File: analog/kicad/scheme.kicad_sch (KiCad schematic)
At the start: 23 parts, among them J1 Barrel_Jack_Switch, U1 LM7805_TO220, U2 LM324

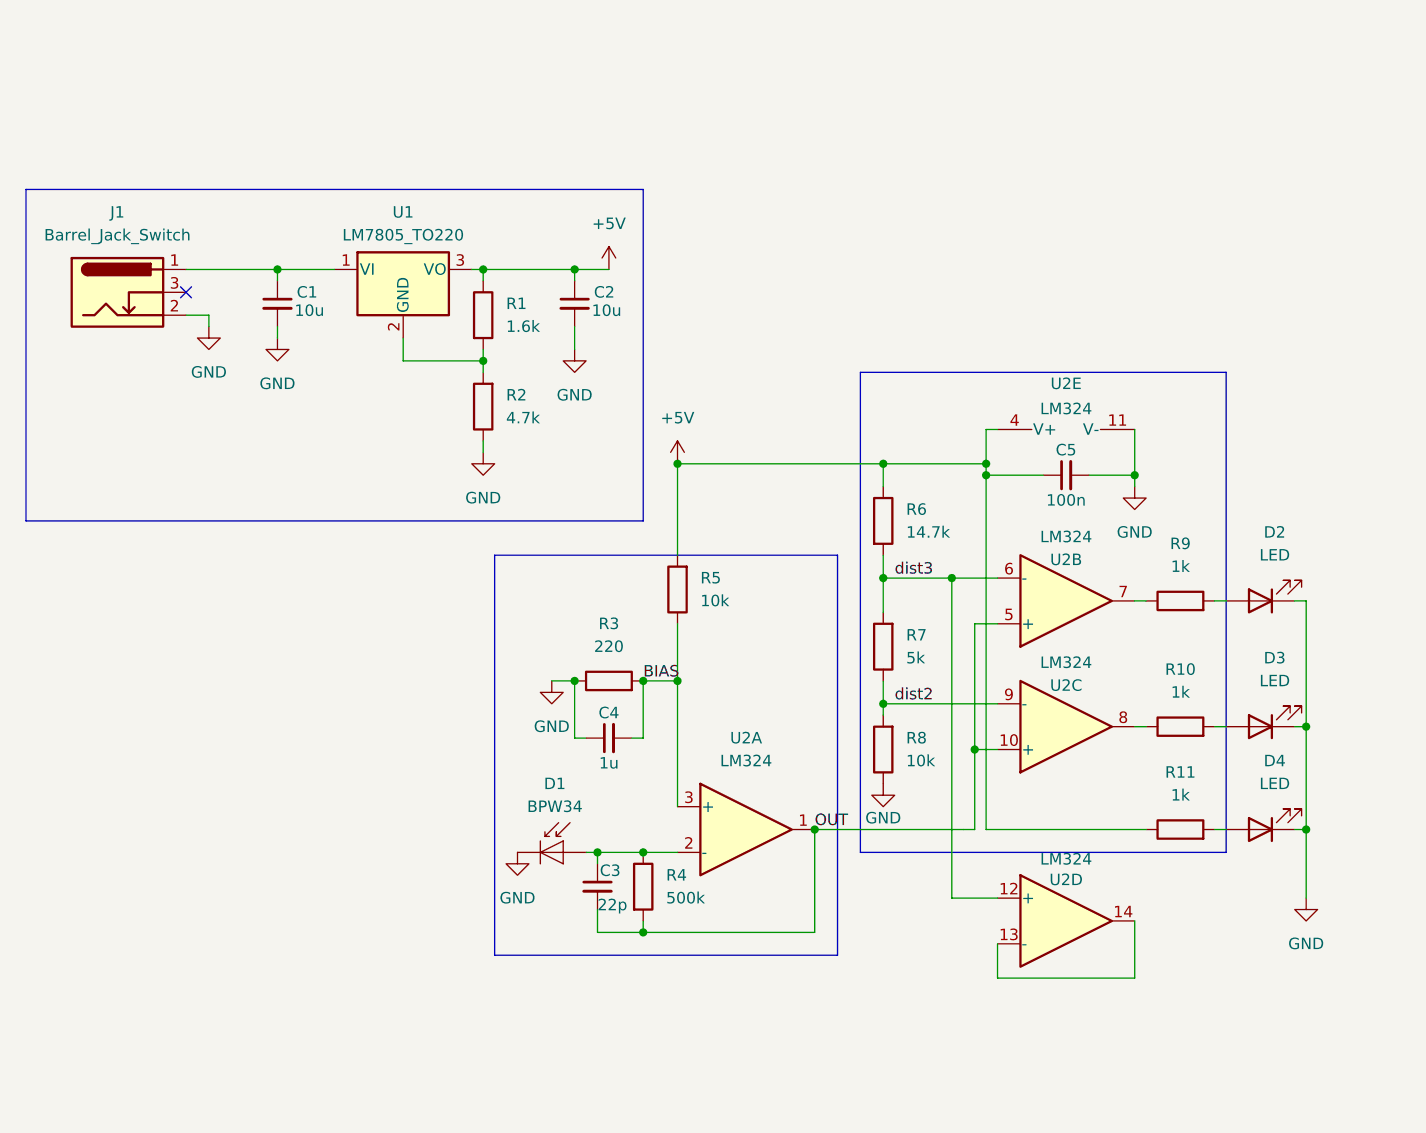
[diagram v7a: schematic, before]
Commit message: pwr good led
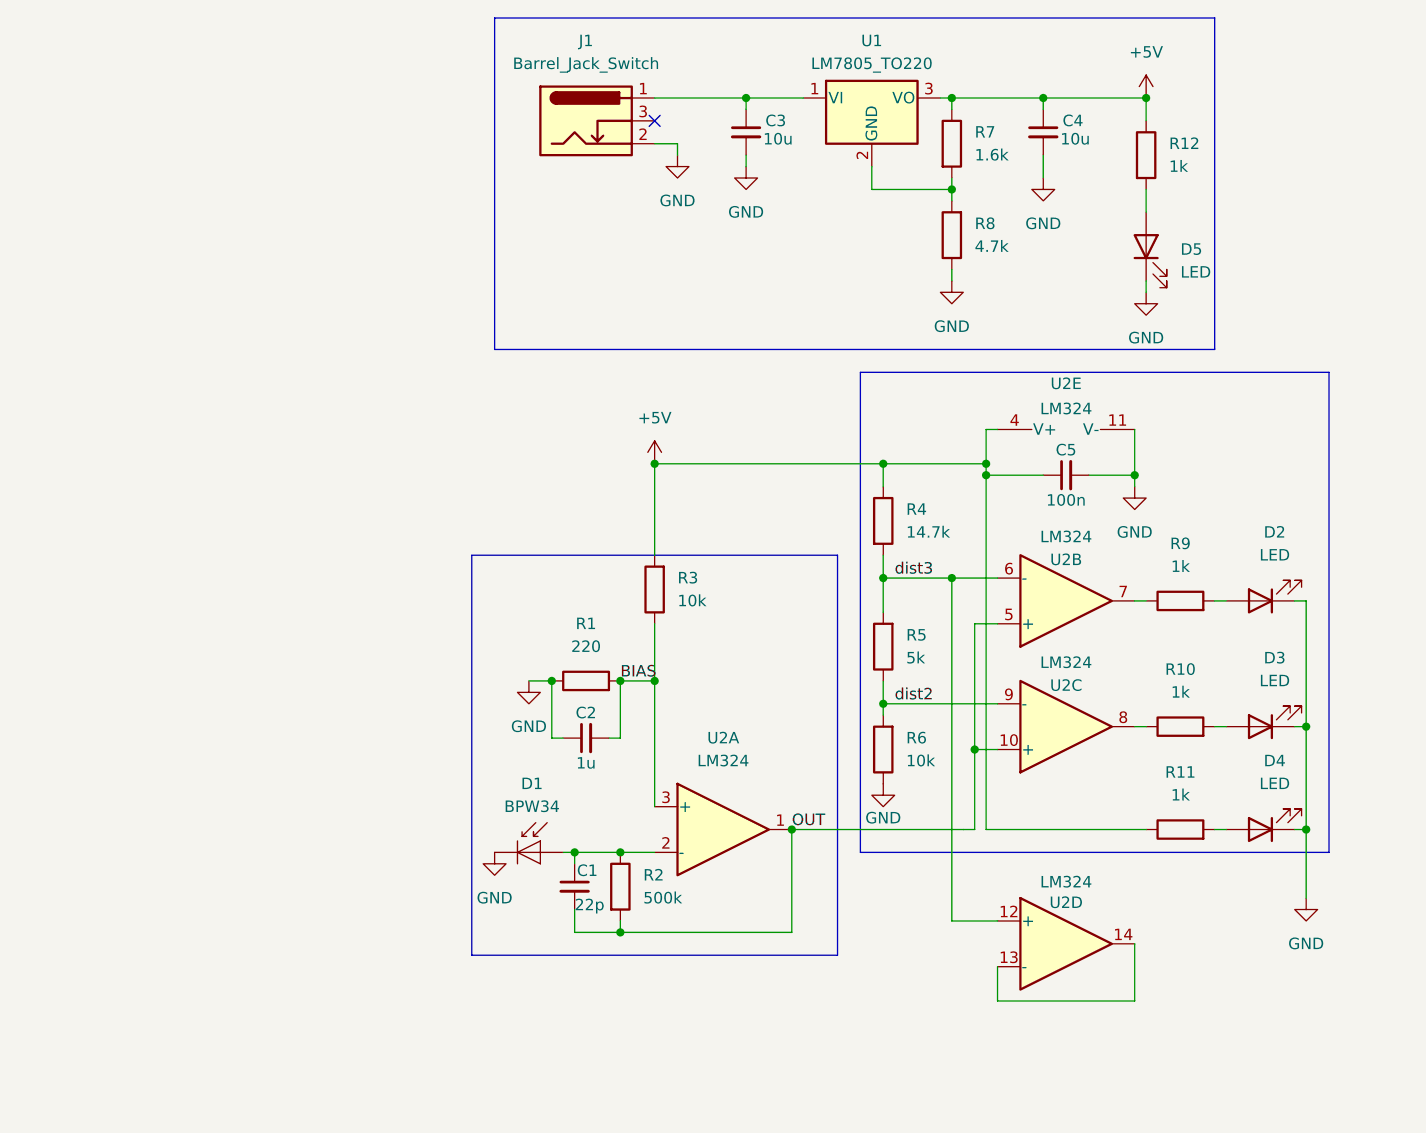
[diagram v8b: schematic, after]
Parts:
- added D5: LED, LED_SMD:LED_0805_2012Metric, symbol Device:LED
- added R12: 1k, Resistor_SMD:R_0805_2012Metric, symbol Device:R
- renumbered C3 to C1, C4 to C2, C1 to C3, C2 to C4, R3 to R1, R4 to R2, R5 to R3, R6 to R4, R7 to R5, R8 to R6, R1 to R7, R2 to R8
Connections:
- net +5V: now also R12.1
- net GND: now also D5.1 (K)
- new net: D5.2 (A), R12.2
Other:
- moved on the sheet: C1, C2, C3, C4, D1, J1, R1, R2, R3, R7, R8, U1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
